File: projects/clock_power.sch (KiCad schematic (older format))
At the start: 7 parts, among them U201 ADM7150

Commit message: updated LED indicators in schematic files (*.sch)
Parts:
- removed D?: LED_G, symbol LED
- added D?: GREEN_LED, symbol GREEN_LED
- added R?: 121, symbol R
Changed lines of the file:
@@
 LIBS:microchip_gosselin
 LIBS:linear_technology_gosselin
+LIBS:led_gosselin
 LIBS:mStereo2-cache
 EELAYER 24 0
@@
 $EndComp
 $Comp
-L LED D?
-U 1 1 544F59C8
-P 7950 4200
-F 0 "D?" H 7950 4300 50  0000 C CNN
-F 1 "LED_G" H 7950 4100 50  0000 C CNN
-F 2 "" H 7950 4200 60  0000 C CNN
-F 3 "" H 7950 4200 60  0000 C CNN
-	1    7950 4200
+L GREEN_LED D?
+U 1 1 5454A7EC
+P 3400 4300
+F 0 "D?" H 3400 4400 50  0000 C CNN
+F 1 "GREEN_LED" H 3400 4200 50  0000 C CNN
+F 2 "" H 3400 4300 60  0000 C CNN
+F 3 "" H 3400 4300 60  0000 C CNN
+F 4 " 160-1423-1-ND" H 3600 4600 60  0001 C CNN "Supplier-PN"
+F 5 "Digi-key" H 3500 4500 60  0001 C CNN "Supplier"
+F 6 "LED GREEN CLEAR THIN 0805 SMD" H 3900 4900 60  0001 C CNN "Description"
+F 7 "Lite-On" H 3700 4700 60  0001 C CNN "Manu"
+F 8 "LTST-C171GKT" H 3800 4800 60  0001 C CNN "Manu-PN"
+	1    3400 4300
 	0    1    1    0
 $EndComp
+$Comp
+L R R?
+U 1 1 5454D1C3
+P 2950 4250
+F 0 "R?" V 3030 4250 40  0000 C CNN
+F 1 "121" V 2957 4251 40  0000 C CNN
+F 2 "" V 2880 4250 30  0000 C CNN
+F 3 "" H 2950 4250 30  0000 C CNN
+F 4 "Digi-key" H 2950 4250 60  0001 C CNN "Supplier"
+F 5 "RNCP0805FTD121RCT-ND" H 2950 4250 60  0001 C CNN "Supplier-PN"
+F 6 "Stackpole" H 2950 4250 60  0001 C CNN "Manu"
+F 7 "RNCP0805FTD121R" H 2950 4250 60  0001 C CNN "Manu-PN"
+F 8 "RES 121 OHM 1/4W 1% 0805" H 2950 4250 60  0001 C CNN "Description"
+	1    2950 4250
+	1    0    0    -1
+$EndComp
 $EndSCHEMATC

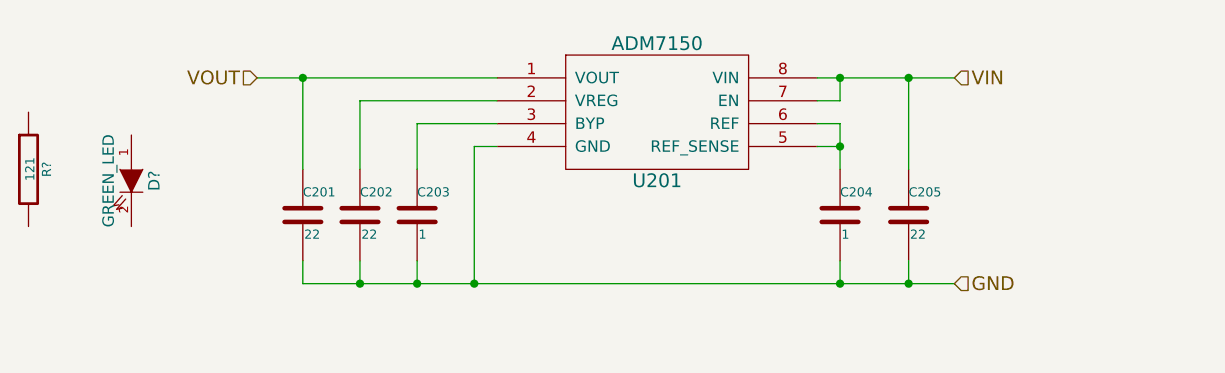
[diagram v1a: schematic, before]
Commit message: updated LEDs in schematic, output connectors, re-annotated
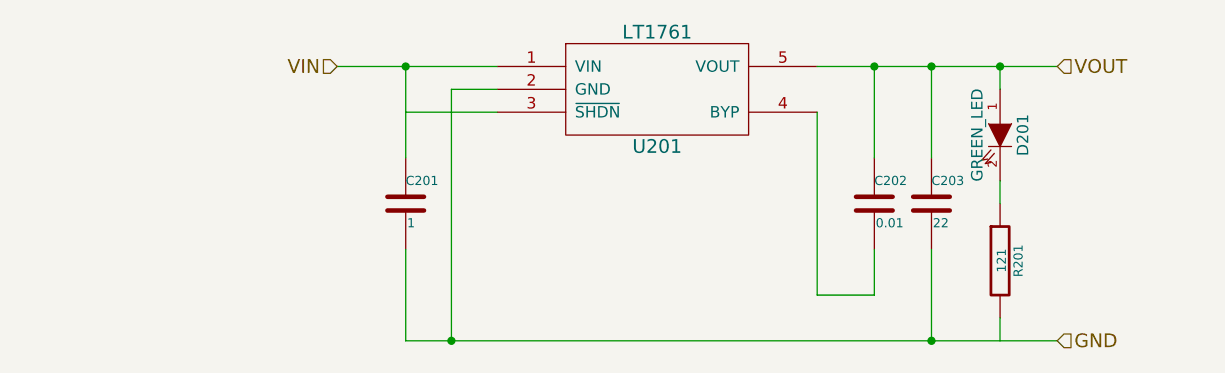
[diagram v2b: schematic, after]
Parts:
- removed C201, C202: 22, symbol C
- removed U201: ADM7150, symbol ADM7150
- added U201: LT1761, symbol LT1761
- C202: renamed from C204; value 1 -> 0.01; Description CAP CER 1UF 16V 10% X7R 0805 -> CAP CER 10000PF 200V X7R 0805; Manu-PN CGJ4J2X7R1C105K125AA -> CGJ4J3X7R2D103K125AA; Supplier-PN 445-8189-1-ND -> 445-9190-1-ND
- gave numbers to parts that had none: 2
- renumbered C203 to C201, C205 to C203
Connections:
- wire segments 21 -> 23
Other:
- moved on the sheet: C201, C202, C203, D201, R201

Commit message: updated power sheets
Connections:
- wire segments 23 -> 17
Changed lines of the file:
@@
 VIN
 Wire Wire Line
-	6400 3800 6650 3800
-Wire Wire Line
-	6650 3800 6900 3800
-Wire Wire Line
-	6900 3800 7200 3800
-Wire Wire Line
-	7200 3800 7450 3800
+	6400 3800 7450 3800
 Text HLabel 7450 5000 2    60   Input ~ 0
 GND
 Wire Wire Line
-	4600 5000 4800 5000
-Wire Wire Line
-	4800 5000 6900 5000
-Wire Wire Line
-	6900 5000 7450 5000
+	4600 5000 7450 5000
 Wire Wire Line
 	4600 3800 4600 4200
@@
 $EndComp
 Wire Wire Line
-	4300 3800 4600 3800
-Wire Wire Line
-	4600 3800 5000 3800
+	4300 3800 5000 3800
 Wire Wire Line
 	5000 4000 4600 4000

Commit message: updated cvpcb footprint/component links
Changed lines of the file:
@@
 Wire Wire Line
 	7200 4300 7200 4400
-Wire Wire Line
-	7200 4900 7200 5000
 $Comp
 L LT1761 U201
@@
 Wire Wire Line
 	4300 3800 5000 3800
-Wire Wire Line
-	5000 4000 4600 4000
 Connection ~ 4600 3800
 Wire Wire Line
@@
 	4600 4600 4600 5000
 Connection ~ 4800 5000
+Wire Wire Line
+	7200 4900 7200 5000
+Connection ~ 7200 5000
+Wire Wire Line
+	5000 4000 4600 4000
+Connection ~ 4600 4000
 $EndSCHEMATC
